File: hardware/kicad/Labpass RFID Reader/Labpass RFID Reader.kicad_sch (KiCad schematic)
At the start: 1 part

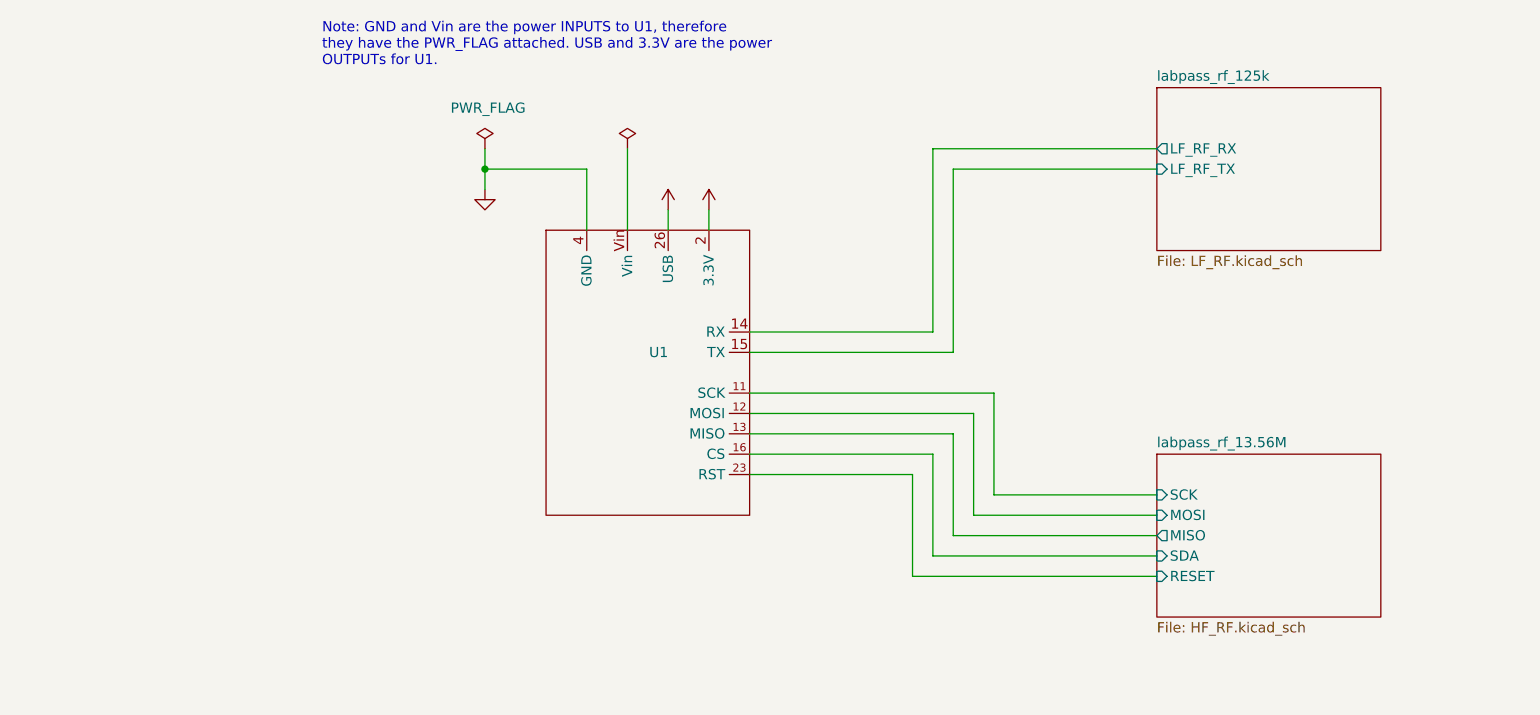
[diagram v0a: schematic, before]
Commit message: Re-do board design using kicad 6.04 stable
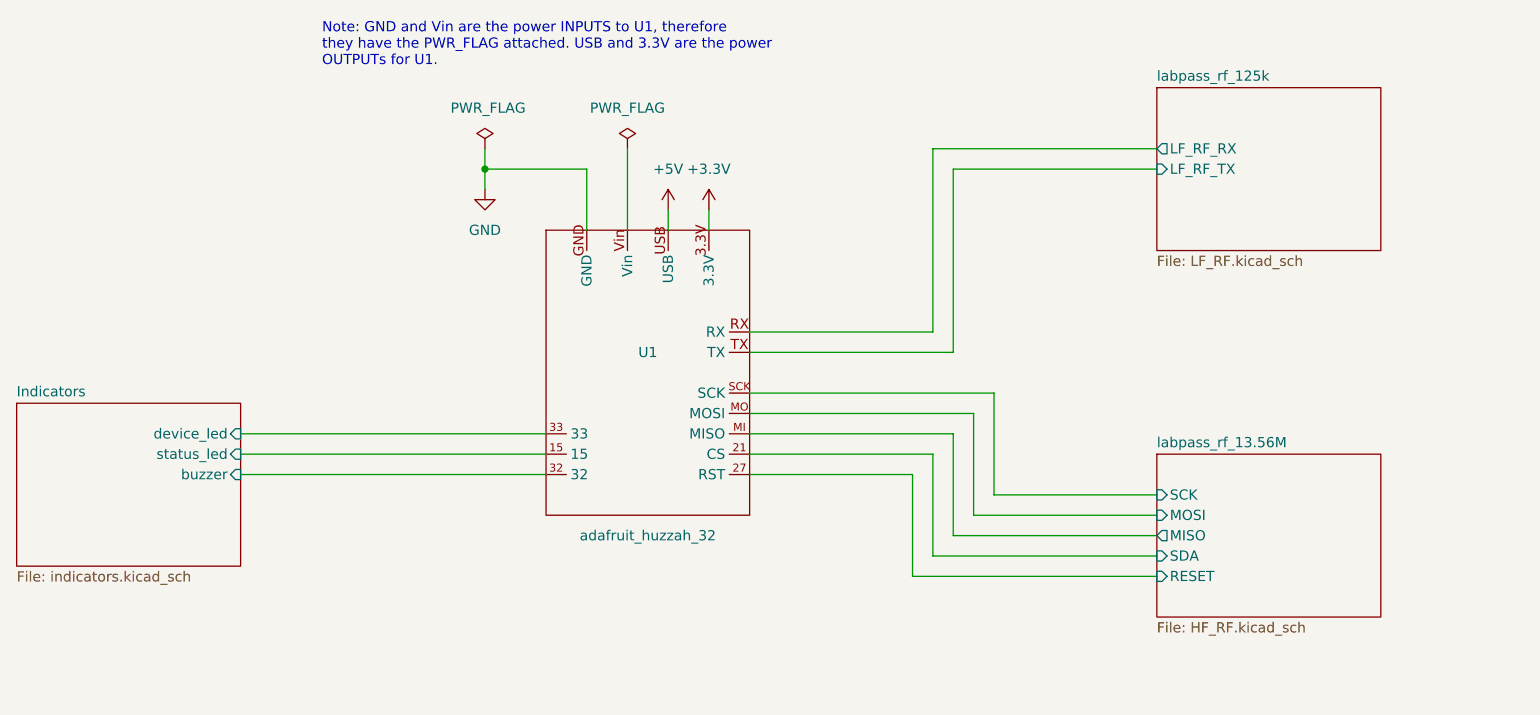
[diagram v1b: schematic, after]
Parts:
- U1: value (none) -> adafruit_huzzah_32; footprint (none) -> Capstone Footprint Library:adafruit_huzzah_32
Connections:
- net +3V3: now also U1.3.3V; no longer U1.2 (3.3V)
- net +5V: now also U1.USB; no longer U1.26 (USB)
- net GND: now also U1.GND; no longer U1.4 (GND)
- net labpass_rf_125k/LF_RF_RX: now also U1.RX; no longer U1.14 (RX)
- net labpass_rf_125k/LF_RF_TX: now also U1.TX; no longer U1.15 (TX)
- net labpass_rf_13.56M/MISO: now also U1.MI (MISO); no longer U1.13 (MISO)
- net labpass_rf_13.56M/MOSI: now also U1.MO (MOSI); no longer U1.12 (MOSI)
- net labpass_rf_13.56M/RESET: now also U1.27 (RST); no longer U1.23 (RST)
- net labpass_rf_13.56M/SCK: now also U1.SCK; no longer U1.11 (SCK)
- net labpass_rf_13.56M/SDA: now also U1.21 (CS); no longer U1.16 (CS)
- new net Indicators/buzzer: U1.32
- new net Indicators/device_led: U1.33
- new net Indicators/status_led: U1.15
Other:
- added sheet Indicators (indicators.kicad_sch)

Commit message: Polish reposition pin headers to clear mez board
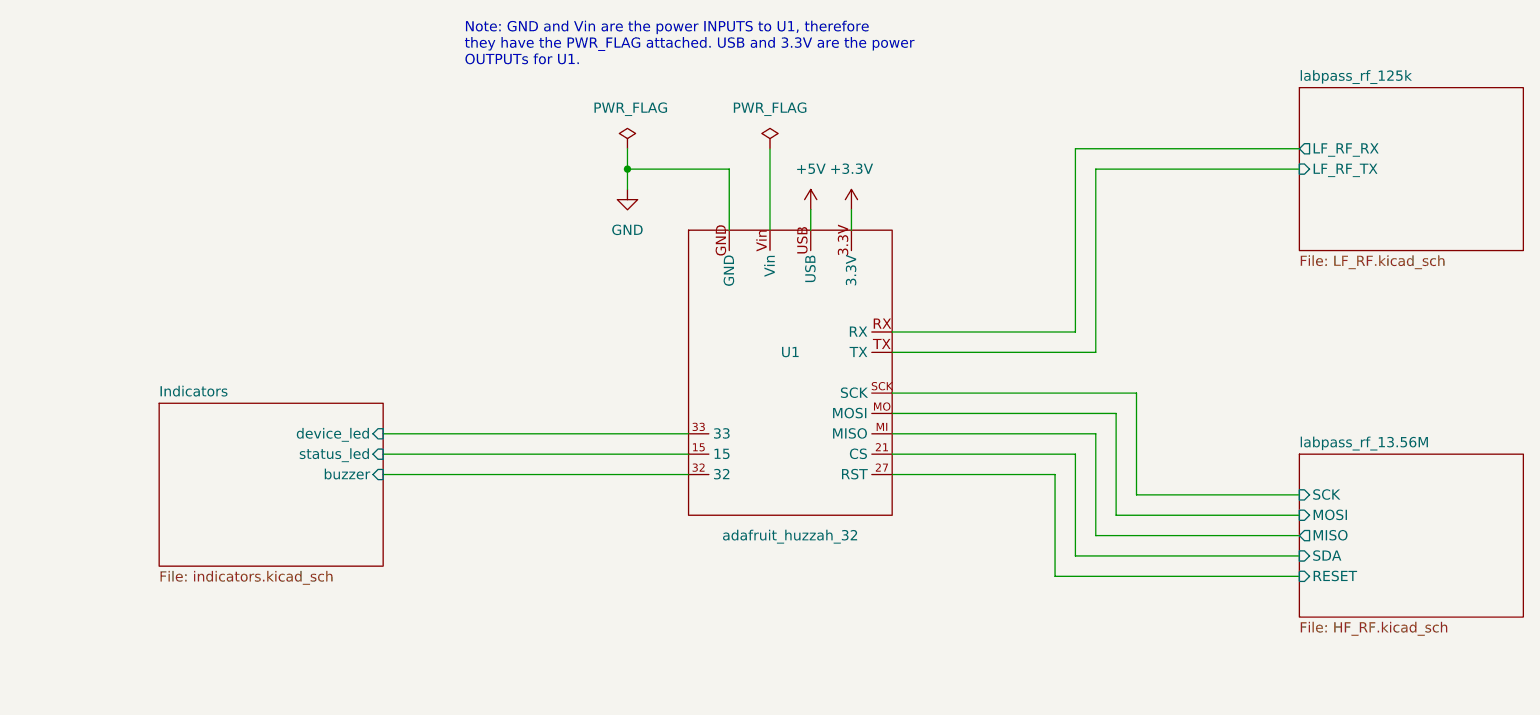
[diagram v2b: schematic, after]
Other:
- moved on the sheet: U1

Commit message: Add RGB LEDs with 4 wires
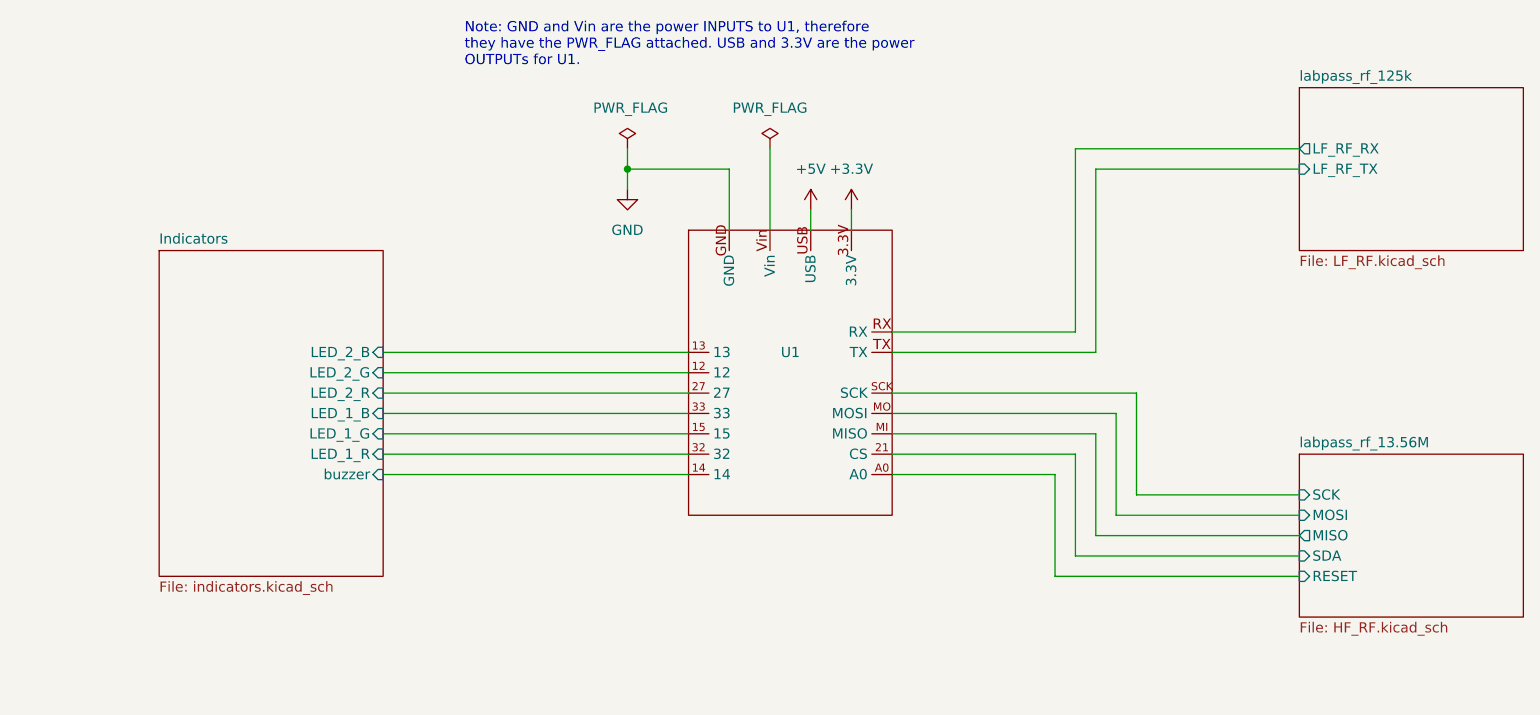
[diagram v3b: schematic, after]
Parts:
- U1: value adafruit_huzzah_32 -> (none); footprint Capstone Footprint Library:adafruit_huzzah_32 -> (none)
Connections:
- net Indicators/buzzer: now also U1.14; no longer U1.32
- net labpass_rf_13.56M/RESET: now also U1.A0; no longer U1.27 (RST)
- net Indicators/device_led renamed Indicators/LED_1_B
- net Indicators/status_led renamed Indicators/LED_1_G
- new net Indicators/LED_1_R: U1.32
- new net Indicators/LED_2_B: U1.13
- new net Indicators/LED_2_G: U1.12
- new net Indicators/LED_2_R: U1.27
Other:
- sheet Indicators ports: added LED_1_B, LED_1_G, LED_1_R, LED_2_B, LED_2_G, LED_2_R; removed device_led, status_led
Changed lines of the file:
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@@
+    (stroke (width 0) (type default) (color 0 0 0 0))
+  )
+  (wire (pts (xy 81.28 106.68) (xy 119.38 106.68))
+    (stroke (width 0) (type default) (color 0 0 0 0))
+  )
+  (wire (pts (xy 170.18 73.66) (xy 195.58 73.66))
+    (stroke (width 0) (type default) (color 0 0 0 0))
+  )
+  (wire (pts (xy 129.54 71.12) (xy 129.54 81.28))
+    (stroke (width 0) (type default) (color 0 0 0 0))
+  )
+  (wire (pts (xy 81.28 96.52) (xy 119.38 96.52))
+    (stroke (width 0) (type default) (color 0 0 0 0))
+  )
+  (wire (pts (xy 175.26 114.3) (xy 175.26 101.6))
+    (stroke (width 0) (type default) (color 0 0 0 0))
+  )
+  (wire (pts (xy 139.7 78.74) (xy 139.7 81.28))
+    (stroke (width 0) (type default) (color 0 0 0 0))
+  )
+  (wire (pts (xy 81.28 104.14) (xy 119.38 104.14))
+    (stroke (width 0) (type default) (color 0 0 0 0))
+  )
+  (wire (pts (xy 165.1 124.46) (xy 195.58 124.46))
+    (stroke (width 0) (type default) (color 0 0 0 0))
+  )
+  (wire (pts (xy 165.1 124.46) (xy 165.1 111.76))
+    (stroke (width 0) (type default) (color 0 0 0 0))
+  )
+  (wire (pts (xy 144.78 111.76) (xy 165.1 111.76))
+    (stroke (width 0) (type default) (color 0 0 0 0))
+  )
+  (wire (pts (xy 170.18 119.38) (xy 170.18 106.68))
+    (stroke (width 0) (type default) (color 0 0 0 0))
+  )
+  (wire (pts (xy 111.76 73.66) (xy 111.76 76.2))
+    (stroke (width 0) (type default) (color 0 0 0 0))
+  )
+  (wire (pts (xy 124.46 81.28) (xy 124.46 73.66))
+    (stroke (width 0) (type default) (color 0 0 0 0))
+  )
+  (wire (pts (xy 144.78 104.14) (xy 172.72 104.14))
+    (stroke (width 0) (type default) (color 0 0 0 0))
+  )
+  (wire (pts (xy 111.76 71.12) (xy 111.76 73.66))
+    (stroke (width 0) (type default) (color 0 0 0 0))
+  )
+  (wire (pts (xy 144.78 109.22) (xy 167.64 109.22))
+    (stroke (width 0) (type default) (color 0 0 0 0))
+  )
+  (wire (pts (xy 172.72 116.84) (xy 172.72 104.14))
+    (stroke (width 0) (type default) (color 0 0 0 0))
+  )
+  (wire (pts (xy 81.28 109.22) (xy 119.38 109.22))
     (stroke (width 0) (type default) (color 0 0 0 0))
   )
@@
     (stroke (width 0) (type default) (color 0 0 0 0))
   )
-  (wire (pts (xy 170.18 73.66) (xy 195.58 73.66))
-    (stroke (width 0) (type default) (color 0 0 0 0))
-  )
-  (wire (pts (xy 129.54 71.12) (xy 129.54 81.28))
-    (stroke (width 0) (type default) (color 0 0 0 0))
-  )
-  (wire (pts (xy 175.26 114.3) (xy 175.26 101.6))
-    (stroke (width 0) (type default) (color 0 0 0 0))
-  )
-  (wire (pts (xy 139.7 78.74) (xy 139.7 81.28))
-    (stroke (width 0) (type default) (color 0 0 0 0))
-  )
-  (wire (pts (xy 165.1 124.46) (xy 195.58 124.46))
-    (stroke (width 0) (type default) (color 0 0 0 0))
-  )
-  (wire (pts (xy 165.1 124.46) (xy 165.1 111.76))
-    (stroke (width 0) (type default) (color 0 0 0 0))
-  )
-  (wire (pts (xy 144.78 111.76) (xy 165.1 111.76))
-    (stroke (width 0) (type default) (color 0 0 0 0))
-  )
-  (wire (pts (xy 170.18 119.38) (xy 170.18 106.68))
-    (stroke (width 0) (type default) (color 0 0 0 0))
-  )
-  (wire (pts (xy 111.76 73.66) (xy 111.76 76.2))
-    (stroke (width 0) (type default) (color 0 0 0 0))
-  )
-  (wire (pts (xy 124.46 81.28) (xy 124.46 73.66))
-    (stroke (width 0) (type default) (color 0 0 0 0))
-  )
-  (wire (pts (xy 144.78 104.14) (xy 172.72 104.14))
-    (stroke (width 0) (type default) (color 0 0 0 0))
-  )
-  (wire (pts (xy 111.76 71.12) (xy 111.76 73.66))
-    (stroke (width 0) (type default) (color 0 0 0 0))
-  )
-  (wire (pts (xy 144.78 109.22) (xy 167.64 109.22))
-    (stroke (width 0) (type default) (color 0 0 0 0))
-  )
-  (wire (pts (xy 172.72 116.84) (xy 172.72 104.14))
-    (stroke (width 0) (type default) (color 0 0 0 0))
-  )
   (wire (pts (xy 170.18 96.52) (xy 170.18 73.66))
     (stroke (width 0) (type default) (color 0 0 0 0))
@@
     (stroke (width 0) (type default) (color 0 0 0 0))
   )
+  (wire (pts (xy 81.28 99.06) (xy 119.38 99.06))
+    (stroke (width 0) (type default) (color 0 0 0 0))
+  )
   (wire (pts (xy 167.64 93.98) (xy 167.64 71.12))
     (stroke (width 0) (type default) (color 0 0 0 0))
@@
     (stroke (width 0) (type default) (color 0 0 0 0))
   )
-  (wire (pts (xy 81.28 106.68) (xy 119.38 106.68))
-    (stroke (width 0) (type default) (color 0 0 0 0))
-  )
   (wire (pts (xy 167.64 121.92) (xy 195.58 121.92))
     (stroke (width 0) (type default) (color 0 0 0 0))
   )
-  (wire (pts (xy 81.28 109.22) (xy 119.38 109.22))
+  (wire (pts (xy 81.28 101.6) (xy 119.38 101.6))
     (stroke (width 0) (type default) (color 0 0 0 0))
   )
@@
     (in_bom yes) (on_board yes)
     (property "Reference" "U1" (id 0) (at 132.08 96.52 0))
-    (property "Value" "adafruit_huzzah_32" (id 1) (at 132.08 119.38 0))
-    (property "Footprint" "Capstone Footprint Library:adafruit_huzzah_32" (id 2) (at 129.54 95.25 0)
+    (property "Value" "" (id 1) (at 132.08 119.38 0))
+    (property "Footprint" "" (id 2) (at 129.54 95.25 0)
       (effects (font (size 1.27 1.27)) hide)
     )
@@
       (effects (font (size 1.27 1.27)) hide)
     )
+    (pin "12")
+    (pin "13")
+    (pin "14")
     (pin "15")
     (pin "21")
@@
     (pin "32")
     (pin "33")
+    (pin "A0")
     (pin "GND")
     (pin "MI")
@@
     (pin "1")
   )
-  (sheet (at 53.34 102.87) (size 27.94 20.32) (fields_autoplaced)
+  (sheet (at 53.34 83.82) (size 27.94 40.64) (fields_autoplaced)
     (stroke (width 0.1524) (type solid) (color 0 0 0 0))
     (fill (color 0 0 0 0.0000))
-    (property "Sheet name" "Indicators" (id 0) (at 53.34 102.1584 0)
+    (property "Sheet name" "Indicators" (id 0) (at 53.34 83.1084 0)
       (effects (font (size 1.27 1.27)) (justify left bottom))
     )
-    (property "Sheet file" "indicators.kicad_sch" (id 1) (at 53.34 123.7746 0)
+    (property "Sheet file" "indicators.kicad_sch" (id 1) (at 53.34 125.0446 0)
       (effects (font (size 1.27 1.27)) (justify left top))
     )
-    (pin "device_led" input (at 81.28 106.68 0)
-      (effects (font (size 1.27 1.27)) (justify right))
-    )
-    (pin "status_led" input (at 81.28 109.22 0)
-      (effects (font (size 1.27 1.27)) (justify right))
-    )
     (pin "buzzer" input (at 81.28 111.76 0)
+      (effects (font (size 1.27 1.27)) (justify right))
+    )
+    (pin "LED_1_R" input (at 81.28 109.22 0)
+      (effects (font (size 1.27 1.27)) (justify right))
+    )
+    (pin "LED_1_G" input (at 81.28 106.68 0)
+      (effects (font (size 1.27 1.27)) (justify right))
+    )
+    (pin "LED_1_B" input (at 81.28 104.14 0)
+      (effects (font (size 1.27 1.27)) (justify right))
+    )
+    (pin "LED_2_R" input (at 81.28 101.6 0)
+      (effects (font (size 1.27 1.27)) (justify right))
+    )
+    (pin "LED_2_G" input (at 81.28 99.06 0)
+      (effects (font (size 1.27 1.27)) (justify right))
+    )
+    (pin "LED_2_B" input (at 81.28 96.52 0)
       (effects (font (size 1.27 1.27)) (justify right))
     )
@@
       (reference "#PWR0101") (unit 1) (value "GND") (footprint "")
     )
-    (path "/0302516d-709c-49c5-8a36-06b29a93bc66/6913b6bf-bc88-486e-8858-19882ae3d368"
+    (path "/0302516d-709c-49c5-8a36-06b29a93bc66/6cbb81c8-2e27-4bcf-b3c5-6e2678aaa087"
       (reference "#PWR0102") (unit 1) (value "GND") (footprint "")
     )
-    (path "/0302516d-709c-49c5-8a36-06b29a93bc66/99108998-9236-49b7-b80f-5c09bdd56c4d"
-      (reference "#PWR0103") (unit 1) (value "GND") (footprint "")
+    (path "/0302516d-709c-49c5-8a36-06b29a93bc66/2f4d6b2b-8ccf-4f14-8b63-a283c9158275"
+      (reference "#PWR0106") (unit 1) (value "GND") (footprint "")
     )
     (path "/0302516d-709c-49c5-8a36-06b29a93bc66/45d6c664-ebc3-467c-b379-3a6d23fa0128"
@@
     )
     (path "/0302516d-709c-49c5-8a36-06b29a93bc66/da07b1c2-c241-4491-9261-cd2de92d1976"
-      (reference "J2") (unit 1) (value "Conn_01x04") (footprint "Connector_PinHeader_1.27mm:PinHeader_1x04_P1.27mm_Vertical_SMD_Pin1Left")
+      (reference "J2") (unit 1) (value "Conn_01x04") (footprint "Connector_PinHeader_1.27mm:PinHeader_1x08_P1.27mm_Vertical_SMD_Pin1Left")
     )
     (path "/7edac1e6-8b57-42c3-be27-8045b1a8bdad/89a031e2-2004-43ba-8e85-2d688c3c9564"
@@
       (reference "R14") (unit 1) (value "R_US") (footprint "Resistor_SMD:R_0603_1608Metric")
     )
-    (path "/0302516d-709c-49c5-8a36-06b29a93bc66/073a338c-b460-4951-ab4f-31e05d61f015"
+    (path "/0302516d-709c-49c5-8a36-06b29a93bc66/831f34f7-bb54-4f24-afae-cc9c189e51b1"
       (reference "R15") (unit 1) (value "R_US") (footprint "Resistor_SMD:R_0603_1608Metric")
     )
-    (path "/0302516d-709c-49c5-8a36-06b29a93bc66/b63049d4-e054-4c57-ae0a-8dee865002eb"
+    (path "/0302516d-709c-49c5-8a36-06b29a93bc66/34585411-f363-4786-a777-d9a8270c15ed"
       (reference "R16") (unit 1) (value "R_US") (footprint "Resistor_SMD:R_0603_1608Metric")
     )
+    (path "/0302516d-709c-49c5-8a36-06b29a93bc66/afb97014-e551-4ba6-b5c5-3015815c1e36"
+      (reference "R17") (unit 1) (value "R_US") (footprint "Resistor_SMD:R_0603_1608Metric")
+    )
+    (path "/0302516d-709c-49c5-8a36-06b29a93bc66/5754bbe5-234f-4b9c-a269-f4a6b6b47c64"
+      (reference "R18") (unit 1) (value "R_US") (footprint "Resistor_SMD:R_0603_1608Metric")
+    )
+    (path "/0302516d-709c-49c5-8a36-06b29a93bc66/4148258a-b81e-4f12-b25b-a8e9f3561359"
+      (reference "R19") (unit 1) (value "R_US") (footprint "Resistor_SMD:R_0603_1608Metric")
+    )
+    (path "/0302516d-709c-49c5-8a36-06b29a93bc66/eafa2acd-2361-4ab6-8b55-c1314761eb8b"
+      (reference "R20") (unit 1) (value "R_US") (footprint "Resistor_SMD:R_0603_1608Metric")
+    )
     (path "/c4ac18a9-c23d-41f2-b747-59286aa6d5d4"

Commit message: last-minute fixes
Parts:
- U1: value (none) -> adafruit_huzzah_32; footprint (none) -> Capstone Footprint Library:adafruit_huzzah_32
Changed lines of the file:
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@@
     (in_bom yes) (on_board yes)
     (property "Reference" "U1" (id 0) (at 132.08 96.52 0))
-    (property "Value" "" (id 1) (at 132.08 119.38 0))
-    (property "Footprint" "" (id 2) (at 129.54 95.25 0)
+    (property "Value" "adafruit_huzzah_32" (id 1) (at 132.08 119.38 0))
+    (property "Footprint" "Capstone Footprint Library:adafruit_huzzah_32" (id 2) (at 129.54 95.25 0)
       (effects (font (size 1.27 1.27)) hide)
     )
